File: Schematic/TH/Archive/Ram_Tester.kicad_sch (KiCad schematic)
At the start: 43 parts, among them J1 Conn_01x02_Pin, J2 ICSP, Q1 2N7000, Q2 2N7000, SW1 SW_DIP_x03, SW2 SW_Push, U1 ATmega328-P, U2 RAM / ZIF, U3 ZIP Socket, Y1 Crystal

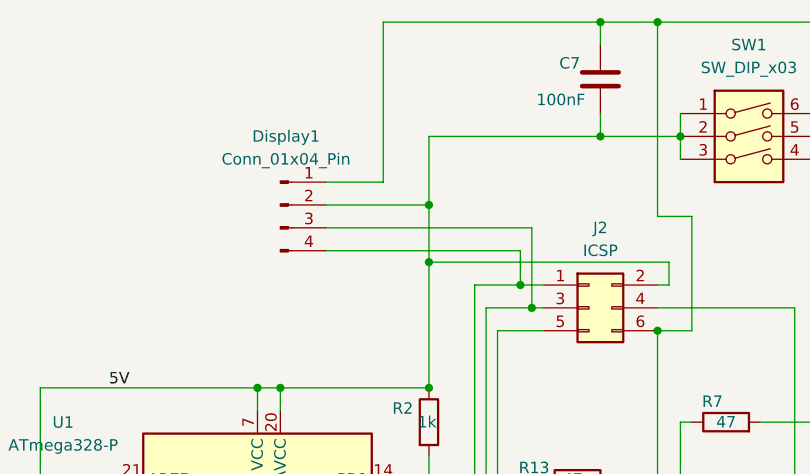
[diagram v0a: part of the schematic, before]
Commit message: v2 TH Version with Display
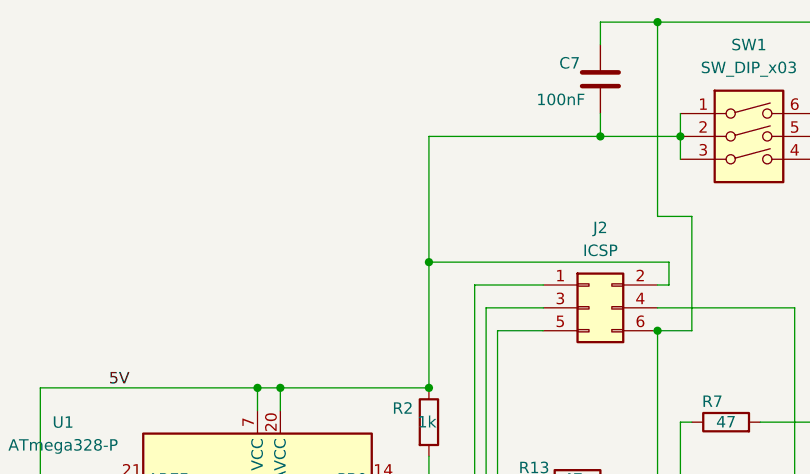
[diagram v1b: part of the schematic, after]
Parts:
- removed Display1: Conn_01x04_Pin, Connector_PinHeader_2.54mm:PinHeader_1x04_P2.54mm_Vertical, symbol Connector:Conn_01x04_Pin
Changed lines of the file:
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@@
 	)
 	(junction
-		(at 100.33 39.37)
-		(diameter 0)
-		(color 0 0 0 0)
-	)
-	(junction
 		(at 57.15 133.35)
 		(diameter 0)
@@
 	)
 	(junction
-		(at 111.76 50.8)
-		(diameter 0)
-		(color 0 0 0 0)
-	)
-	(junction
 		(at 134.62 151.13)
 		(diameter 0)
@@
 	)
 	(junction
-		(at 119.38 19.05)
-		(diameter 0)
-		(color 0 0 0 0)
-	)
-	(junction
 		(at 252.73 102.87)
 		(diameter 0)
@@
 	)
 	(junction
-		(at 110.49 48.26)
-		(diameter 0)
-		(color 0 0 0 0)
-	)
-	(junction
 		(at 157.48 31.75)
 		(diameter 0)
@@
 	(wire
 		(pts
-			(xy 95.25 36.83) (xy 88.9 36.83)
-		)
-		(stroke
-			(width 0)
-			(type default)
-		)
-	)
-	(wire
-		(pts
 			(xy 220.98 50.8) (xy 234.95 50.8)
 		)
@@
 	(wire
 		(pts
-			(xy 100.33 31.75) (xy 100.33 39.37)
+			(xy 100.33 31.75) (xy 100.33 45.72)
 		)
 		(stroke
@@
 	(wire
 		(pts
-			(xy 111.76 50.8) (xy 106.68 50.8)
-		)
-		(stroke
-			(width 0)
-			(type default)
-		)
-	)
-	(wire
-		(pts
-			(xy 88.9 44.45) (xy 110.49 44.45)
-		)
-		(stroke
-			(width 0)
-			(type default)
-		)
-	)
-	(wire
-		(pts
 			(xy 121.92 140.97) (xy 121.92 143.51)
 		)
@@
 	(wire
 		(pts
-			(xy 95.25 19.05) (xy 95.25 36.83)
-		)
-		(stroke
-			(width 0)
-			(type default)
-		)
-	)
-	(wire
-		(pts
 			(xy 57.15 142.24) (xy 57.15 143.51)
 		)
@@
 	(wire
 		(pts
-			(xy 110.49 44.45) (xy 110.49 48.26)
-		)
-		(stroke
-			(width 0)
-			(type default)
-		)
-	)
-	(wire
-		(pts
 			(xy 100.33 59.69) (xy 83.82 59.69)
 		)
@@
 	(wire
 		(pts
-			(xy 119.38 19.05) (xy 95.25 19.05)
-		)
-		(stroke
-			(width 0)
-			(type default)
-		)
-	)
-	(wire
-		(pts
 			(xy 142.24 82.55) (xy 142.24 160.02)
 		)
@@
 	(wire
 		(pts
-			(xy 111.76 41.91) (xy 111.76 50.8)
-		)
-		(stroke
-			(width 0)
-			(type default)
-		)
-	)
-	(wire
-		(pts
 			(xy 254 127) (xy 278.13 127)
 		)
@@
 	(wire
 		(pts
-			(xy 100.33 39.37) (xy 100.33 45.72)
-		)
-		(stroke
-			(width 0)
-			(type default)
-		)
-	)
-	(wire
-		(pts
 			(xy 96.52 118.11) (xy 106.68 118.11)
 		)
@@
 	(wire
 		(pts
-			(xy 110.49 48.26) (xy 105.41 48.26)
-		)
-		(stroke
-			(width 0)
-			(type default)
-		)
-	)
-	(wire
-		(pts
 			(xy 43.18 142.24) (xy 43.18 143.51)
 		)
@@
 	(wire
 		(pts
-			(xy 88.9 41.91) (xy 111.76 41.91)
-		)
-		(stroke
-			(width 0)
-			(type default)
-		)
-	)
-	(wire
-		(pts
 			(xy 100.33 31.75) (xy 119.38 31.75)
 		)
@@
 	(wire
 		(pts
-			(xy 113.03 50.8) (xy 111.76 50.8)
+			(xy 113.03 50.8) (xy 106.68 50.8)
 		)
 		(stroke
@@
 	(wire
 		(pts
-			(xy 88.9 39.37) (xy 100.33 39.37)
-		)
-		(stroke
-			(width 0)
-			(type default)
-		)
-	)
-	(wire
-		(pts
 			(xy 267.97 72.39) (xy 267.97 78.74)
 		)
@@
 	(wire
 		(pts
-			(xy 113.03 48.26) (xy 110.49 48.26)
+			(xy 113.03 48.26) (xy 105.41 48.26)
 		)
 		(stroke
@@
 		)
 		(instances
-			(project "Ram_Tester"
+			(project ""
 				(path "/9a90cd34-b6db-44ec-969f-9bfdcecefc17"
 					(reference "U3")
@@
 		)
 		(instances
-			(project "Ram_Tester"
+			(project ""
 				(path "/9a90cd34-b6db-44ec-969f-9bfdcecefc17"
 					(reference "Y1")
@@
 		)
 		(instances
-			(project "Ram_Tester"
+			(project ""
 				(path "/9a90cd34-b6db-44ec-969f-9bfdcecefc17"
 					(reference "F1")
@@
 		)
 		(instances
-			(project "Ram_Tester"
+			(project ""
 				(path "/9a90cd34-b6db-44ec-969f-9bfdcecefc17"
 					(reference "C3")
@@
 		)
 		(instances
-			(project "Ram_Tester"
+			(project ""
 				(path "/9a90cd34-b6db-44ec-969f-9bfdcecefc17"
 					(reference "R7")
@@
 		)
 		(instances
-			(project "Ram_Tester"
+			(project ""
 				(path "/9a90cd34-b6db-44ec-969f-9bfdcecefc17"
 					(reference "J2")
@@
 		)
 		(instances
-			(project "Ram_Tester"
+			(project ""
 				(path "/9a90cd34-b6db-44ec-969f-9bfdcecefc17"
 					(reference "SW1")
@@
 		)
 		(instances
-			(project "Ram_Tester"
+			(project ""
 				(path "/9a90cd34-b6db-44ec-969f-9bfdcecefc17"
 					(reference "U2")
@@
 		)
 		(instances
-			(project "Ram_Tester"
+			(project ""
 				(path "/9a90cd34-b6db-44ec-969f-9bfdcecefc17"
 					(reference "D1")
@@
 		)
 		(instances
-			(project "Ram_Tester"
+			(project ""
 				(path "/9a90cd34-b6db-44ec-969f-9bfdcecefc17"
 					(reference "Q1")
@@
 	)
 	(symbol
-		(lib_id "Connector:Conn_01x04_Pin")
-		(at 83.82 39.37 0)
-		(unit 1)
-		(exclude_from_sim no)
-		(in_bom yes)
-		(on_board yes)
-		(dnp no)
-		(fields_autoplaced yes)
-		(property "Reference" "Display1"
-			(at 84.455 31.75 0)
-			(effects
-				(font
-					(size 1.27 1.27)
-				)
-			)
-		)
-		(property "Value" "Conn_01x04_Pin"
-			(at 84.455 34.29 0)
-			(effects
-				(font
-					(size 1.27 1.27)
-				)
-			)
-		)
-		(property "Footprint" "Connector_PinHeader_2.54mm:PinHeader_1x04_P2.54mm_Vertical"
-			(at 83.82 39.37 0)
-			(effects
-				(font
-					(size 1.27 1.27)
-				)
-				(hide yes)
-			)
-		)
-		(property "Datasheet" "~"
-			(at 83.82 39.37 0)
-			(effects
-				(font
-					(size 1.27 1.27)
-				)
-				(hide yes)
-			)
-		)
-		(property "Description" "Generic connector, single row, 01x04, script generated"
-			(at 83.82 39.37 0)
-			(effects
-				(font
-					(size 1.27 1.27)
-				)
-				(hide yes)
-			)
-		)
-		(pin "1"
-		)
-		(pin "4"
-		)
-		(pin "2"
-		)
-		(pin "3"
-		)
-		(instances
-			(project "Ram_Tester"
-				(path "/9a90cd34-b6db-44ec-969f-9bfdcecefc17"
-					(reference "Display1")
-					(unit 1)
-				)
-			)
-		)
-	)
-	(symbol
 		(lib_id "Device:R")
 		(at 110.49 123.19 90)
@@
 		)
 		(instances
-			(project "Ram_Tester"
+			(project ""
 				(path "/9a90cd34-b6db-44ec-969f-9bfdcecefc17"
 					(reference "C5")
@@
 		)
 		(instances
-			(project "Ram_Tester"
+			(project ""
 				(path "/9a90cd34-b6db-44ec-969f-9bfdcecefc17"
 					(reference "C2")
@@
 		)
 		(instances
-			(project "Ram_Tester"
+			(project ""
 				(path "/9a90cd34-b6db-44ec-969f-9bfdcecefc17"
 					(reference "J1")
@@
 		)
 		(instances
-			(project "Ram_Tester"
+			(project ""
 				(path "/9a90cd34-b6db-44ec-969f-9bfdcecefc17"
 					(reference "SW2")
@@
 		)
 		(instances
-			(project "Ram_Tester"
+			(project ""
 				(path "/9a90cd34-b6db-44ec-969f-9bfdcecefc17"
 					(reference "U1")
@@
 		)
 		(instances
-			(project "Ram_Tester"
+			(project ""
 				(path "/9a90cd34-b6db-44ec-969f-9bfdcecefc17"
 					(reference "C1")
